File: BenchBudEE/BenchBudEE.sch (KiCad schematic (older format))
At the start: 0 parts

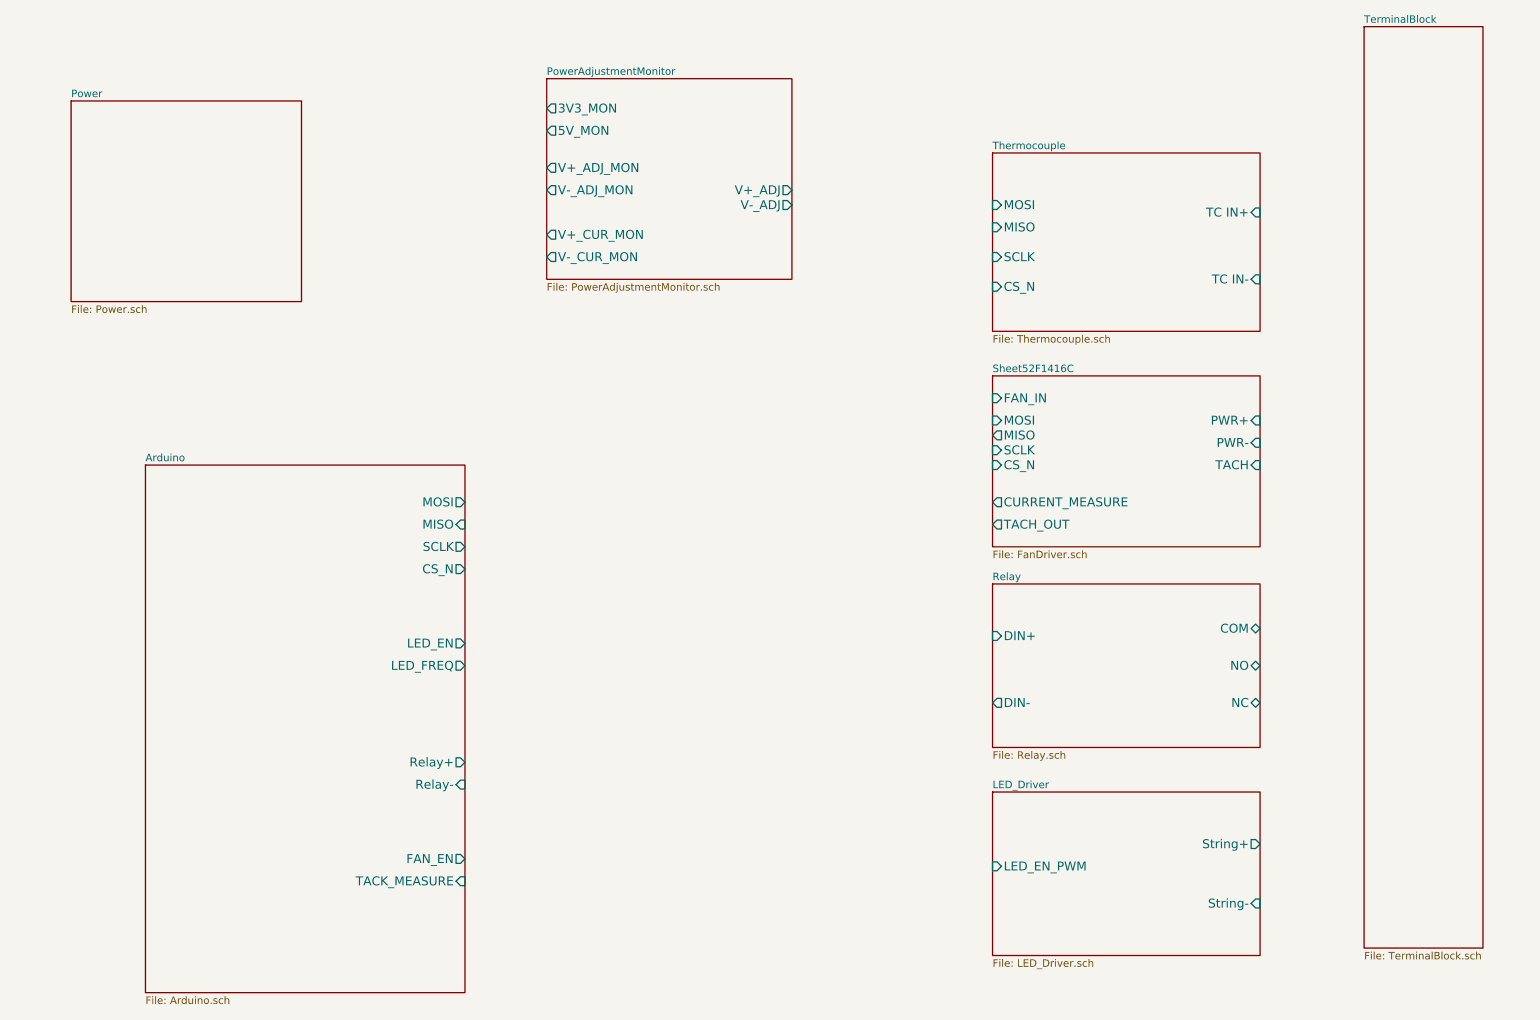
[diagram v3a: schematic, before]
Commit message: Schematic modules connected together and to arduino pins
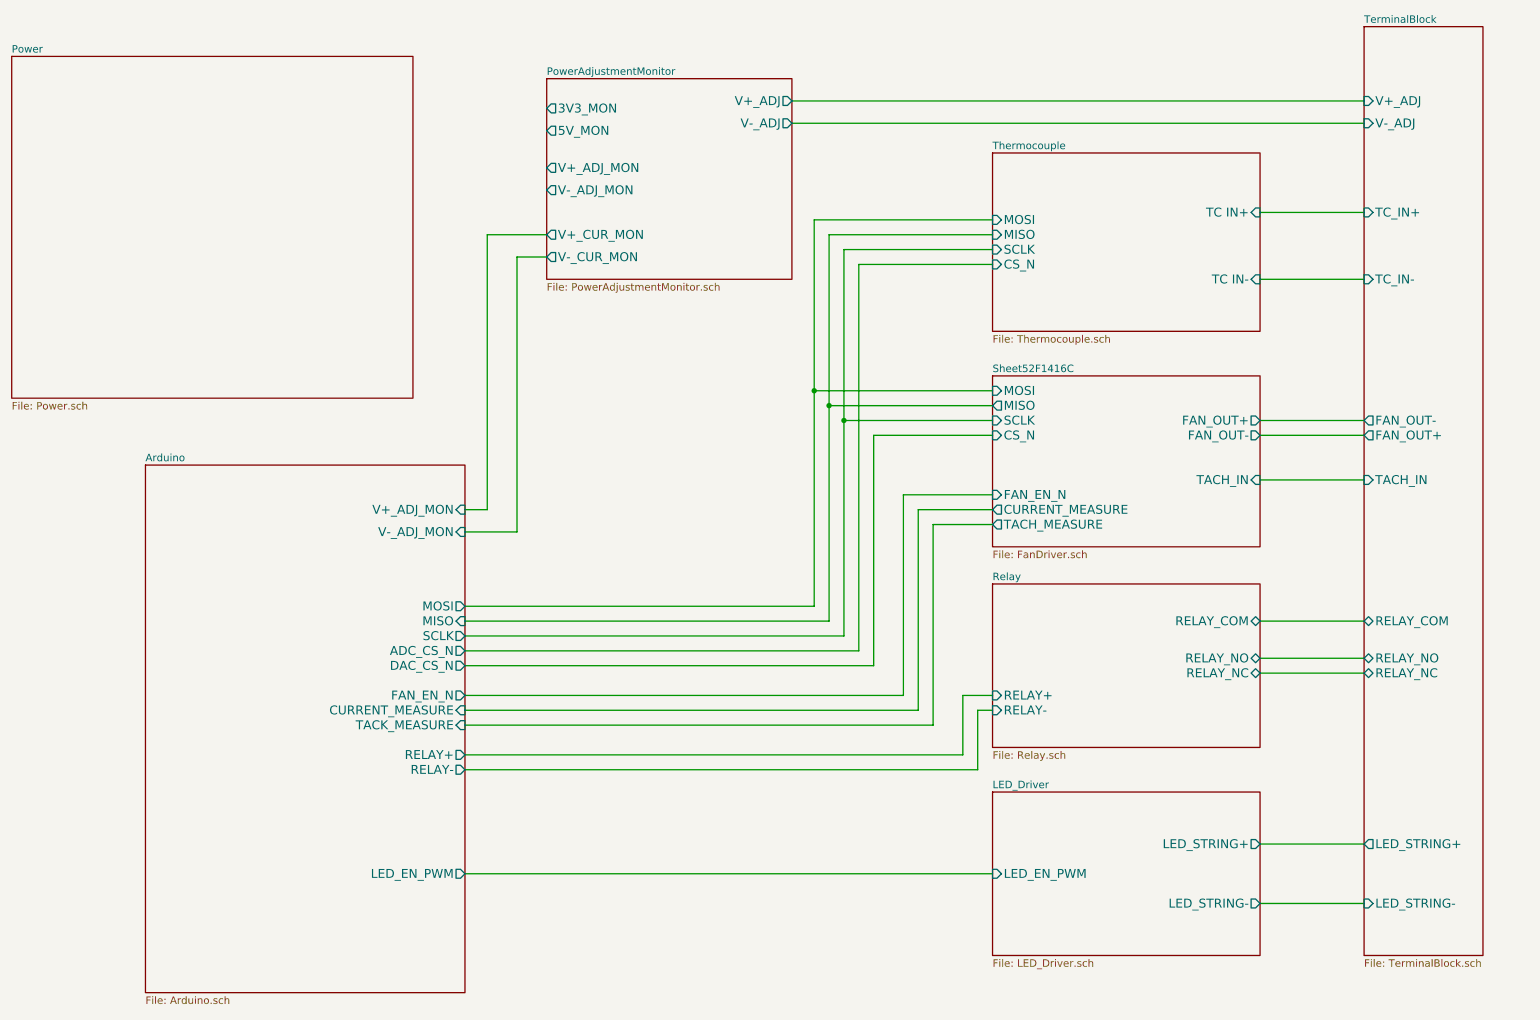
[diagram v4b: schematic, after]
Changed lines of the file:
@@
 LIBS:valves
 LIBS:CE Library
+LIBS:atx_24pin_power
 LIBS:BenchBudEE-cache
 EELAYER 27 0
@@
 Sheet 1 9
 Title ""
-Date "6 feb 2014"
+Date "8 feb 2014"
 Rev ""
 Comp ""
@@
 $EndDescr
 $Sheet
-S 1750 3600 2150 3550
-U 52F141E3
-F0 "Arduino" 50
-F1 "Arduino.sch" 50
-F2 "MOSI" O R 3900 3850 60
-F3 "MISO" I R 3900 4000 60
-F4 "SCLK" O R 3900 4150 60
-F5 "CS_N" O R 3900 4300 60
-F6 "Relay+" O R 3900 5600 60
-F7 "Relay-" I R 3900 5750 60
-F8 "LED_EN" O R 3900 4800 60
-F9 "LED_FREQ" O R 3900 4950 60
-F10 "FAN_EN" O R 3900 6250 60
-F11 "TACK_MEASURE" I R 3900 6400 60
-$EndSheet
-$Sheet
 S 7450 4400 1800 1100
 U 52F1423A
 F0 "Relay" 50
 F1 "Relay.sch" 50
-F2 "DIN+" I L 7450 4750 60
-F3 "DIN-" O L 7450 5200 60
-F4 "NO" B R 9250 4950 60
-F5 "NC" B R 9250 5200 60
-F6 "COM" B R 9250 4700 60
+F2 "RELAY_NO" B R 9250 4900 60
+F3 "RELAY_NC" B R 9250 5000 60
+F4 "RELAY_COM" B R 9250 4650 60
+F5 "RELAY+" I L 7450 5150 60
+F6 "RELAY-" I L 7450 5250 60
 $EndSheet
 $Sheet
@@
 F0 "LED_Driver" 50
 F1 "LED_Driver.sch" 50
-F2 "String+" O R 9250 6150 60
-F3 "String-" I R 9250 6550 60
-F4 "LED_EN_PWM" I L 7450 6300 60
-$EndSheet
-$Sheet
-S 9950 650  800  6200
+F2 "LED_EN_PWM" I L 7450 6350 60
+F3 "LED_STRING+" O R 9250 6150 60
+F4 "LED_STRING-" O R 9250 6550 60
+$EndSheet
+$Sheet
+S 9950 650  800  6250
 U 52F142CF
 F0 "TerminalBlock" 50
 F1 "TerminalBlock.sch" 50
-$EndSheet
-$Sheet
-S 1250 1150 1550 1350
+F2 "V+_ADJ" I L 9950 1150 60
+F3 "V-_ADJ" I L 9950 1300 60
+F4 "FAN_OUT+" O L 9950 3400 60
+F5 "FAN_OUT-" O L 9950 3300 60
+F6 "TACH_IN" I L 9950 3700 60
+F7 "LED_STRING+" O L 9950 6150 60
+F8 "LED_STRING-" I L 9950 6550 60
+F9 "TC_IN+" I L 9950 1900 60
+F10 "TC_IN-" I L 9950 2350 60
+F11 "RELAY_COM" B L 9950 4650 60
+F12 "RELAY_NO" B L 9950 4900 60
+F13 "RELAY_NC" B L 9950 5000 60
+$EndSheet
+$Sheet
+S 850  850  2700 2300
 U 52F14318
 F0 "Power" 50
@@
 F0 "Sheet52F1416C" 50
 F1 "FanDriver.sch" 50
-F2 "PWR+" I R 9250 3300 60
-F3 "PWR-" I R 9250 3450 60
-F4 "FAN_IN" I L 7450 3150 60
-F5 "TACH" I R 9250 3600 60
-F6 "TACH_OUT" O L 7450 4000 60
-F7 "CURRENT_MEASURE" O L 7450 3850 60
-F8 "MOSI" I L 7450 3300 60
-F9 "MISO" O L 7450 3400 60
-F10 "SCLK" I L 7450 3500 60
-F11 "CS_N" I L 7450 3600 60
+F2 "CURRENT_MEASURE" O L 7450 3900 60
+F3 "MOSI" I L 7450 3100 60
+F4 "MISO" O L 7450 3200 60
+F5 "SCLK" I L 7450 3300 60
+F6 "CS_N" I L 7450 3400 60
+F7 "TACH_IN" I R 9250 3700 60
+F8 "TACH_MEASURE" O L 7450 4000 60
+F9 "FAN_OUT+" O R 9250 3300 60
+F10 "FAN_OUT-" O R 9250 3400 60
+F11 "FAN_EN_N" I L 7450 3800 60
 $EndSheet
 $Sheet
@@
 F2 "TC IN+" I R 9250 1900 60
 F3 "TC IN-" I R 9250 2350 60
-F4 "MISO" I L 7450 2000 60
-F5 "MOSI" I L 7450 1850 60
-F6 "SCLK" I L 7450 2200 60
-F7 "CS_N" I L 7450 2400 60
+F4 "MISO" I L 7450 2050 60
+F5 "MOSI" I L 7450 1950 60
+F6 "SCLK" I L 7450 2150 60
+F7 "CS_N" I L 7450 2250 60
 $EndSheet
 $Sheet
@@
 F0 "PowerAdjustmentMonitor" 50
 F1 "PowerAdjustmentMonitor.sch" 50
-F2 "V+_ADJ" O R 6100 1750 60
-F3 "V-_ADJ" O R 6100 1850 60
+F2 "V+_ADJ" O R 6100 1150 60
+F3 "V-_ADJ" O R 6100 1300 60
 F4 "3V3_MON" O L 4450 1200 60
 F5 "5V_MON" O L 4450 1350 60
@@
 F9 "V-_CUR_MON" O L 4450 2200 60
 $EndSheet
+Wire Wire Line
+	6100 1300 9950 1300
+Wire Wire Line
+	6100 1150 9950 1150
+Wire Wire Line
+	9250 3300 9950 3300
+Wire Wire Line
+	9950 3400 9250 3400
+Wire Wire Line
+	9250 3700 9950 3700
+Wire Wire Line
+	9250 2350 9950 2350
+Wire Wire Line
+	9950 1900 9250 1900
+Wire Wire Line
+	9250 5000 9950 5000
+Wire Wire Line
+	9950 4900 9250 4900
+Wire Wire Line
+	9250 4650 9950 4650
+Wire Wire Line
+	9250 6150 9950 6150
+Wire Wire Line
+	9250 6550 9950 6550
+Wire Wire Line
+	3900 3900 4050 3900
+Wire Wire Line
+	4050 3900 4050 2050
+Wire Wire Line
+	4050 2050 4450 2050
+Wire Wire Line
+	4450 2200 4250 2200
+Wire Wire Line
+	4250 2200 4250 4050
+Wire Wire Line
+	4250 4050 3900 4050
+Wire Wire Line
+	6250 1950 6250 4550
+Wire Wire Line
+	6250 1950 7450 1950
+Wire Wire Line
+	6350 2050 6350 4650
+Wire Wire Line
+	6450 2150 6450 4750
+Wire Wire Line
+	6550 2250 6550 4850
+Wire Wire Line
+	7450 3100 6250 3100
+Connection ~ 6250 3100
+Wire Wire Line
+	7450 3200 6350 3200
+Connection ~ 6350 3200
+Wire Wire Line
+	7450 3300 6450 3300
+Connection ~ 6450 3300
+Wire Wire Line
+	6950 5250 6950 3900
+Wire Wire Line
+	6950 3900 7450 3900
+Wire Wire Line
+	7450 4000 7050 4000
+Wire Wire Line
+	7050 4000 7050 5350
+Wire Wire Line
+	7450 3400 6650 3400
+Wire Wire Line
+	6650 3400 6650 4950
+Wire Wire Line
+	6550 4850 3900 4850
+Wire Wire Line
+	6650 4950 3900 4950
+Wire Wire Line
+	6250 4550 3900 4550
+Wire Wire Line
+	7450 2050 6350 2050
+Wire Wire Line
+	6450 2150 7450 2150
+Wire Wire Line
+	7450 2250 6550 2250
+Wire Wire Line
+	6350 4650 3900 4650
+Wire Wire Line
+	6450 4750 3900 4750
+Wire Wire Line
+	7450 3800 6850 3800
+Wire Wire Line
+	6850 3800 6850 5150
+Wire Wire Line
+	6850 5150 3900 5150
+Wire Wire Line
+	6950 5250 3900 5250
+Wire Wire Line
+	7050 5350 3900 5350
+$Sheet
+S 1750 3600 2150 3550
+U 52F141E3
+F0 "Arduino" 50
+F1 "Arduino.sch" 50
+F2 "MOSI" O R 3900 4550 60
+F3 "MISO" I R 3900 4650 60
+F4 "SCLK" O R 3900 4750 60
+F5 "TACK_MEASURE" I R 3900 5350 60
+F6 "FAN_EN_N" O R 3900 5150 60
+F7 "RELAY+" O R 3900 5550 60
+F8 "RELAY-" O R 3900 5650 60
+F9 "LED_EN_PWM" O R 3900 6350 60
+F10 "CURRENT_MEASURE" I R 3900 5250 60
+F11 "V+_ADJ_MON" I R 3900 3900 60
+F12 "V-_ADJ_MON" I R 3900 4050 60
+F13 "DAC_CS_N" O R 3900 4950 60
+F14 "ADC_CS_N" O R 3900 4850 60
+$EndSheet
+Wire Wire Line
+	3900 5550 7250 5550
+Wire Wire Line
+	7250 5550 7250 5150
+Wire Wire Line
+	7250 5150 7450 5150
+Wire Wire Line
+	7450 5250 7350 5250
+Wire Wire Line
+	7350 5250 7350 5650
+Wire Wire Line
+	7350 5650 3900 5650
+Wire Wire Line
+	3900 6350 7450 6350
 $EndSCHEMATC

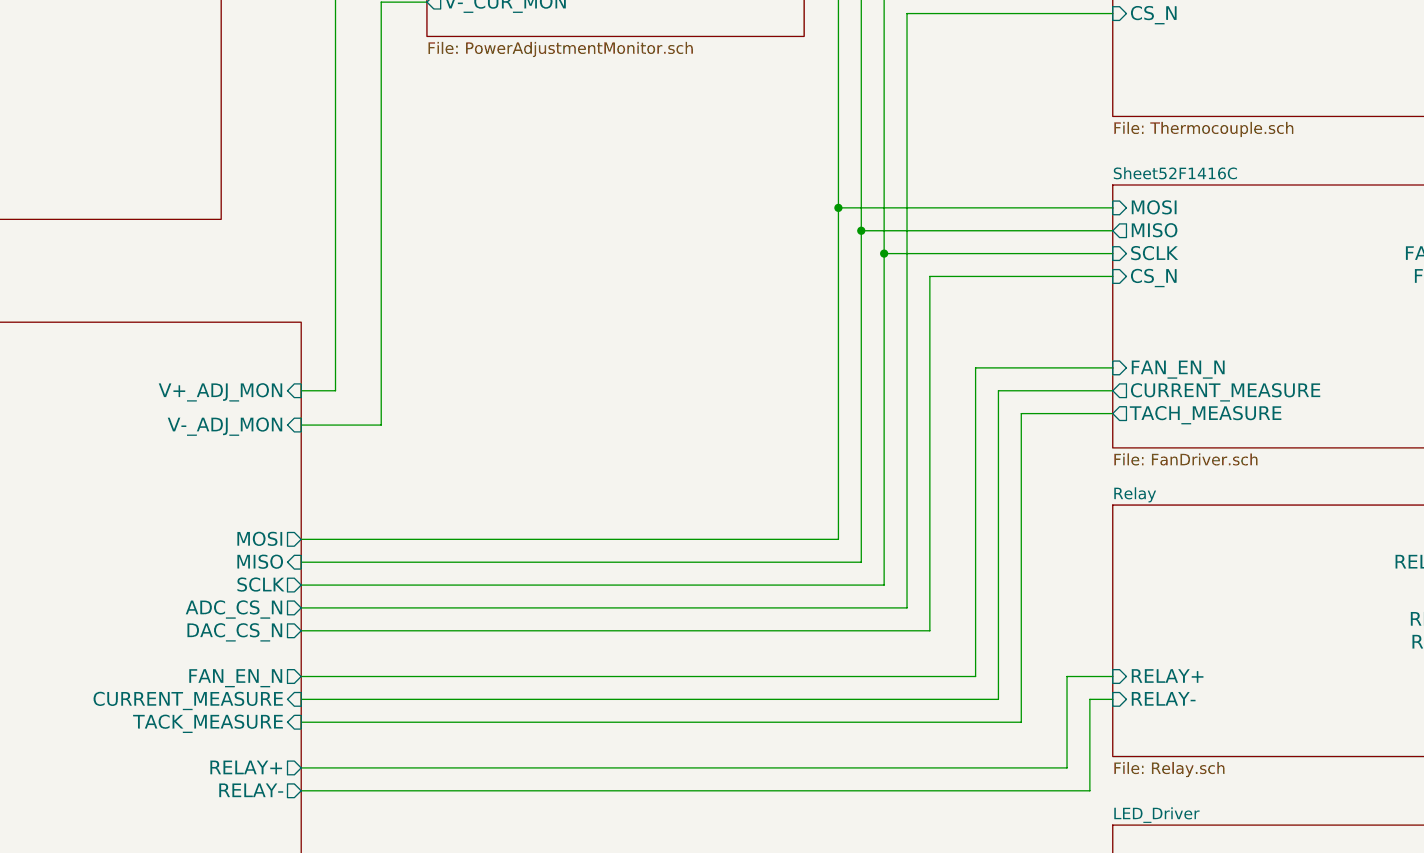
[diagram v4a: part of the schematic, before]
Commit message: Parts added to relay module. Schematic tidied up.
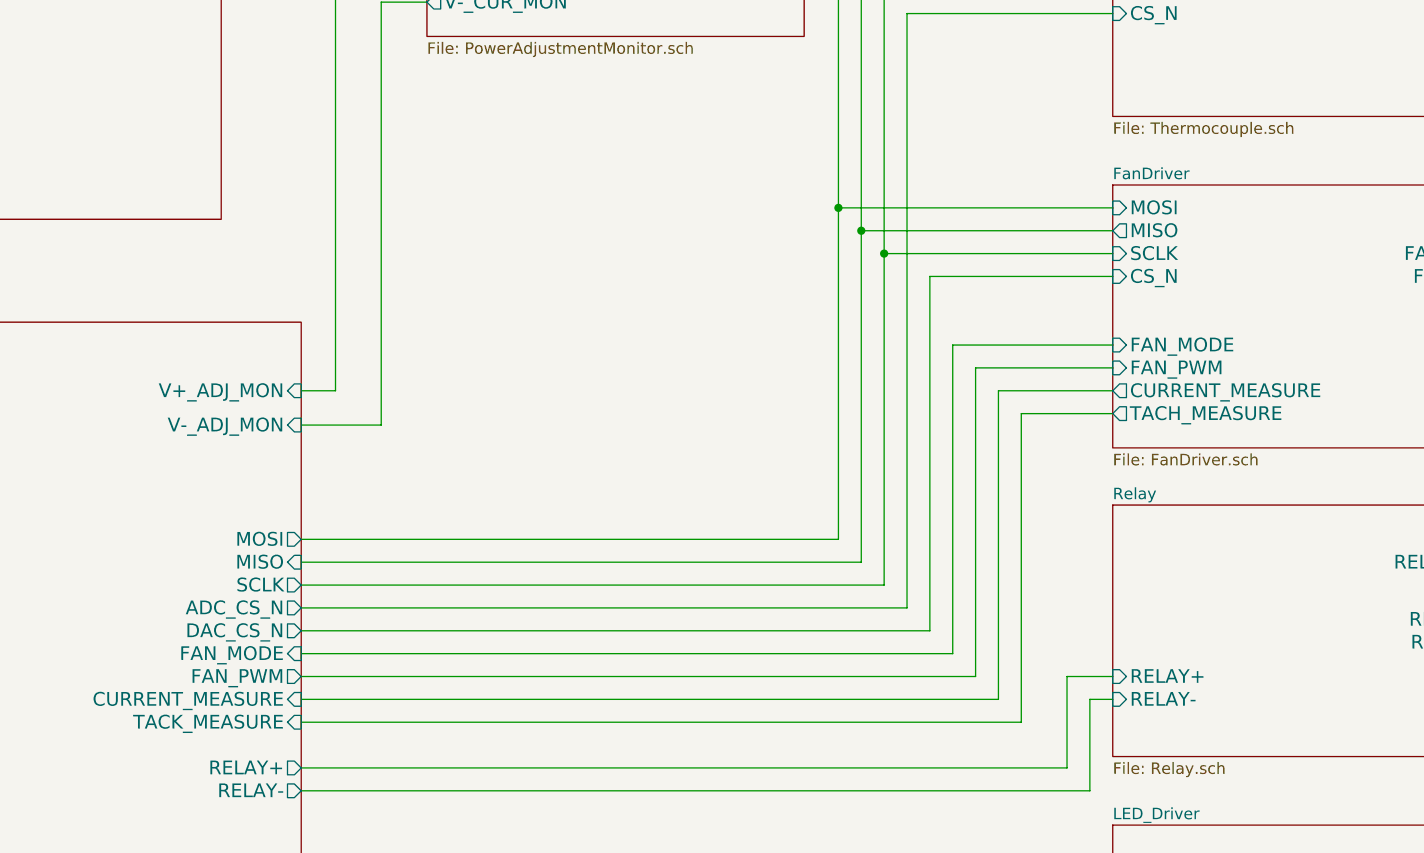
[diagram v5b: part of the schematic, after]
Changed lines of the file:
@@
 Sheet 1 9
 Title ""
-Date "8 feb 2014"
+Date "19 feb 2014"
 Rev ""
 Comp ""
@@
 S 7450 3000 1800 1150
 U 52F1416D
-F0 "Sheet52F1416C" 50
+F0 "FanDriver" 50
 F1 "FanDriver.sch" 50
 F2 "CURRENT_MEASURE" O L 7450 3900 60
@@
 F9 "FAN_OUT+" O R 9250 3300 60
 F10 "FAN_OUT-" O R 9250 3400 60
-F11 "FAN_EN_N" I L 7450 3800 60
+F11 "FAN_MODE" I L 7450 3700 60
+F12 "FAN_PWM" I L 7450 3800 60
 $EndSheet
 $Sheet
@@
 F4 "SCLK" O R 3900 4750 60
 F5 "TACK_MEASURE" I R 3900 5350 60
-F6 "FAN_EN_N" O R 3900 5150 60
-F7 "RELAY+" O R 3900 5550 60
-F8 "RELAY-" O R 3900 5650 60
-F9 "LED_EN_PWM" O R 3900 6350 60
-F10 "CURRENT_MEASURE" I R 3900 5250 60
-F11 "V+_ADJ_MON" I R 3900 3900 60
-F12 "V-_ADJ_MON" I R 3900 4050 60
-F13 "DAC_CS_N" O R 3900 4950 60
-F14 "ADC_CS_N" O R 3900 4850 60
+F6 "RELAY+" O R 3900 5550 60
+F7 "RELAY-" O R 3900 5650 60
+F8 "LED_EN_PWM" O R 3900 6350 60
+F9 "CURRENT_MEASURE" I R 3900 5250 60
+F10 "V+_ADJ_MON" I R 3900 3900 60
+F11 "V-_ADJ_MON" I R 3900 4050 60
+F12 "DAC_CS_N" O R 3900 4950 60
+F13 "ADC_CS_N" O R 3900 4850 60
+F14 "FAN_PWM" O R 3900 5150 60
+F15 "FAN_MODE" I R 3900 5050 60
 $EndSheet
 Wire Wire Line
@@
 Wire Wire Line
 	3900 6350 7450 6350
+Wire Wire Line
+	3900 5050 6750 5050
+Wire Wire Line
+	6750 5050 6750 3700
+Wire Wire Line
+	6750 3700 7450 3700
 $EndSCHEMATC
